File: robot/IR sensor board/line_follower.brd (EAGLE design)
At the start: 8 parts

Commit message: updated schematic and board
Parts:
- JP1: device pinhead:1_05X2MM -> pinhead:1X05
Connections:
- net N$4: now also JP1.2; no longer JP1.3
- net N$5: now also JP1.3; no longer JP1.2
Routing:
- net VCC: track 74.1 -> 70.2 mm
- net GND: track 2.60 -> 0.00 mm
- net N$6: track 18.9 -> 18.2 mm
- net N$4: track 27.1 -> 26.6 mm
- removed copper zone on layer 16, net N$9

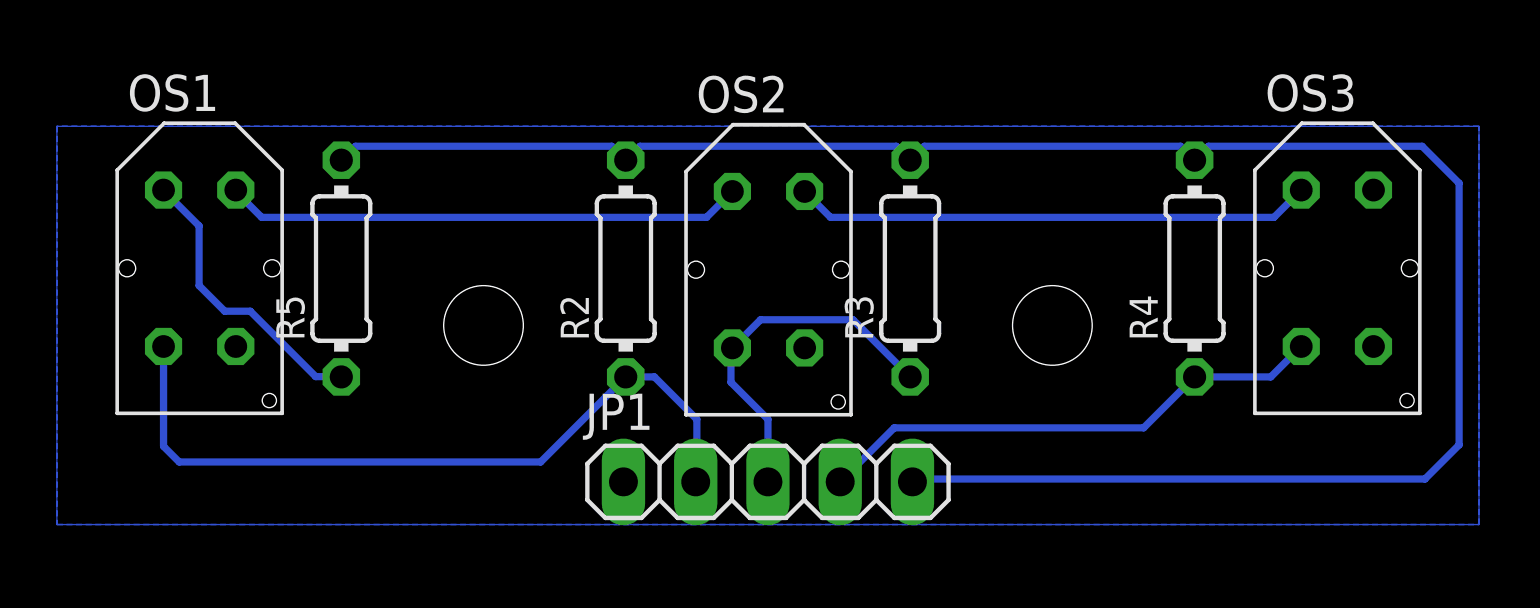
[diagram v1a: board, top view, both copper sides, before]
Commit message: updated sensor board
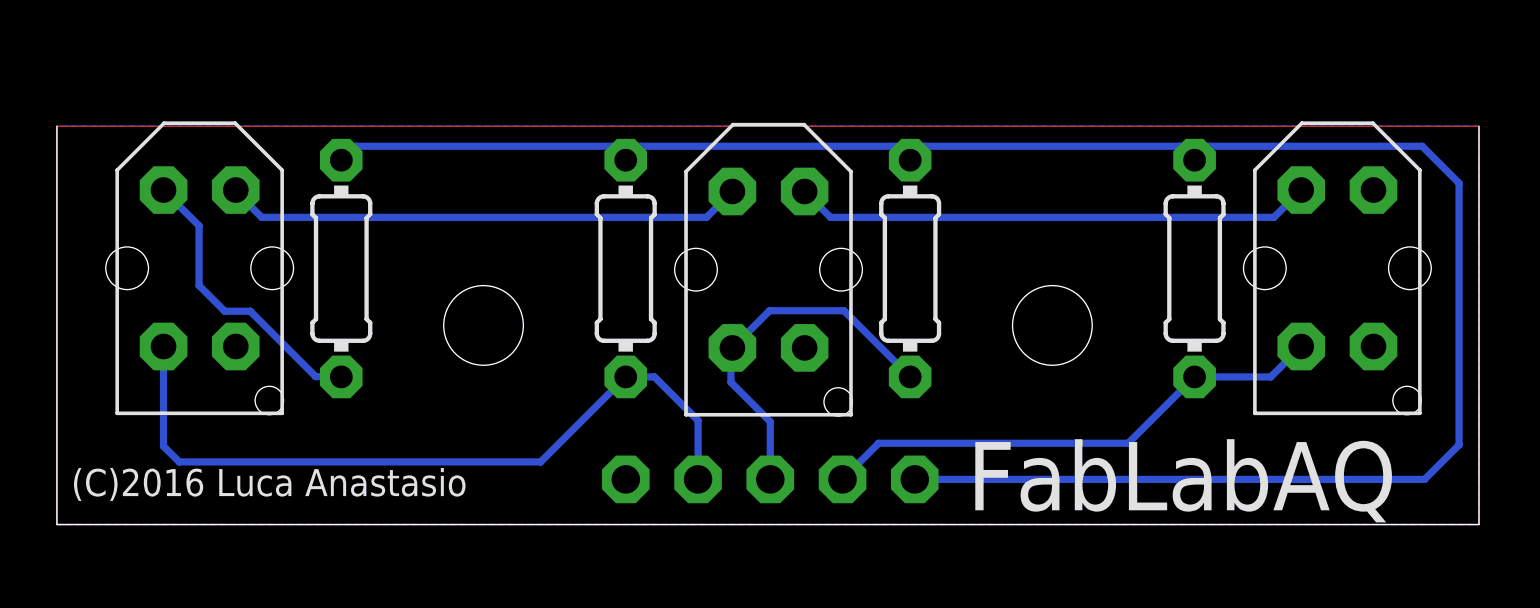
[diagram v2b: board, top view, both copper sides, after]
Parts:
- removed R5: (no value), resistor:0204/7
- added JP2, JP3, JP4, JP5: (no value), pinhead1:1X01
- added R1: 27R, resistor1:0204/7
- JP1: device pinhead:1X05 -> pinhead1:1X01
- R2, R3, R4: value (none) -> 10K; device resistor:0204/7 -> resistor1:0204/7
- moved JP1 5.00 mm to (20.0, 1.59), flipped to the bottom, turned to 90 degrees
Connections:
- net N$3: now also R1.1; no longer R5.1
- net N$4: now also JP2.1; no longer JP1.2
- net N$5: now also JP3.1; no longer JP1.3
- net N$6: now also JP4.1; no longer JP1.4
- net VCC: now also JP5.1, R1.2; no longer JP1.5, R5.2
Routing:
- net N$8: track 0.00 -> 128.0 mm
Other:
- board outline added: 50 x 14 mm
- board text added: "(C)2016 Luca Anastasio"
- board text added: "FabLabAQ"
- board text added: "GND"
- board text added: "VCC"
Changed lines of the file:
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@@
 <setting verticaltext="up"/>
 </settings>
-<grid distance="0.1" unitdist="mm" unit="mm" style="lines" multiple="1" display="no" altdistance="0.025" altunitdist="inch" altunit="inch"/>
+<grid distance="0.5" unitdist="mm" unit="mm" style="lines" multiple="1" display="yes" altdistance="0.025" altunitdist="inch" altunit="inch"/>
 <layers>
 <layer number="1" name="Top" color="4" fill="1" visible="yes" active="yes"/>
@@
 <hole x="15" y="7" drill="2.8"/>
 <hole x="35" y="7" drill="2.8"/>
+<text x="21.2725" y="3.175" size="0.8128" layer="22" font="vector" ratio="10" rot="MR0">GND</text>
+<text x="31.4325" y="3.175" size="0.8128" layer="22" font="vector" ratio="10" rot="MR0">VCC</text>
+<wire x1="0" y1="0" x2="50" y2="0" width="0" layer="46"/>
+<wire x1="50" y1="0" x2="50" y2="14" width="0" layer="46"/>
+<wire x1="0" y1="14" x2="0" y2="0" width="0" layer="46"/>
+<wire x1="0" y1="0" x2="50" y2="0" width="0" layer="47"/>
+<wire x1="50" y1="0" x2="50" y2="14" width="0" layer="47"/>
+<wire x1="50" y1="14" x2="0" y2="14" width="0" layer="47"/>
+<wire x1="0" y1="14" x2="0" y2="0" width="0" layer="47"/>
+<text x="0.5" y="1" size="0.95" layer="21" font="vector" ratio="10">(C)2016 Luca Anastasio</text>
+<text x="32" y="0.5" size="2.4" layer="21" font="vector" ratio="12">FabLabAQ</text>
+<wire x1="0" y1="0" x2="50" y2="0" width="0" layer="48"/>
+<wire x1="50" y1="0" x2="50" y2="14" width="0" layer="48"/>
+<wire x1="50" y1="14" x2="0" y2="14" width="0" layer="48"/>
+<wire x1="0" y1="14" x2="0" y2="0" width="0" layer="48"/>
 </plain>
 <attributes>
@@
 </autorouter>
 <elements>
-<element name="OS1" library="tcrt5000" package="TCRT5000" value="" x="5.02" y="9.01" rot="R270"/>
-<element name="OS2" library="tcrt5000" package="TCRT5000" value="" x="25.02" y="8.96" rot="R270"/>
-<element name="OS3" library="tcrt5000" package="TCRT5000" value="" x="45.02" y="9.01" rot="R270"/>
-<element name="R2" library="resistor" package="0204/7" value="" x="20" y="9" rot="R90"/>
-<element name="R3" library="resistor" package="0204/7" value="" x="30" y="9" rot="R90"/>
-<element name="R4" library="resistor" package="0204/7" value="" x="40" y="9" rot="R90"/>
-<element name="R5" library="resistor" package="0204/7" value="" x="10" y="9" rot="R90"/>
-<element name="JP1" library="pinhead" package="1X05" value="" x="25" y="1.5"/>
+<element name="OS1" library="tcrt5000" package="TCRT5000" value="" x="5.02" y="9.01" smashed="yes" rot="R270">
+<attribute name="VALUE" x="2.48" y="2.31" size="1.27" layer="21"/>
+</element>
+<element name="OS2" library="tcrt5000" package="TCRT5000" value="" x="25.02" y="8.96" smashed="yes" rot="R270">
+<attribute name="VALUE" x="22.48" y="2.26" size="1.27" layer="21"/>
+</element>
+<element name="OS3" library="tcrt5000" package="TCRT5000" value="" x="45.02" y="9.01" smashed="yes" rot="R270">
+<attribute name="VALUE" x="42.48" y="2.31" size="1.27" layer="21"/>
+</element>
+<element name="R2" library="resistor1" package="0204/7" value="10K" x="20" y="9" smashed="yes" rot="R90">
+<attribute name="VALUE" x="20.4826" y="7.3744" size="0.9906" layer="27" font="vector" ratio="10" rot="R90"/>
+</element>
+<element name="R3" library="resistor1" package="0204/7" value="10K" x="30" y="9" smashed="yes" rot="R90">
+<attribute name="VALUE" x="30.4826" y="7.3744" size="0.9906" layer="27" font="vector" ratio="10" rot="R90"/>
+</element>
+<element name="R4" library="resistor1" package="0204/7" value="10K" x="40" y="9" smashed="yes" rot="R90">
+<attribute name="VALUE" x="40.4826" y="7.3744" size="0.9906" layer="27" font="vector" ratio="10" rot="R90"/>
+</element>
+<element name="R1" library="resistor1" package="0204/7" value="27R" x="10" y="9" smashed="yes" rot="R90">
+<attribute name="VALUE" x="10.4826" y="7.3744" size="0.9906" layer="27" font="vector" ratio="10" rot="R90"/>
+</element>
+<element name="JP1" library="pinhead1" package="1X01" value="" x="20.0025" y="1.5875" smashed="yes" rot="MR90">
+<attribute name="VALUE" x="16.8275" y="0.3175" size="1.27" layer="28" rot="MR90"/>
+</element>
+<element name="JP2" library="pinhead1" package="1X01" value="" x="22.5425" y="1.5875" smashed="yes" rot="MR180">
+<attribute name="VALUE" x="21.2725" y="4.7625" size="1.27" layer="28" rot="MR180"/>
+</element>
+<element name="JP3" library="pinhead1" package="1X01" value="" x="25.0825" y="1.5875" smashed="yes" rot="MR180">
+<attribute name="VALUE" x="23.8125" y="4.7625" size="1.27" layer="28" rot="MR180"/>
+</element>
+<element name="JP4" library="pinhead1" package="1X01" value="" x="27.6225" y="1.5875" smashed="yes" rot="MR180">
+<attribute name="VALUE" x="26.3525" y="4.7625" size="1.27" layer="28" rot="MR180"/>
+</element>
+<element name="JP5" library="pinhead1" package="1X01" value="" x="30.1625" y="1.5875" smashed="yes" rot="MR270">
+<attribute name="VALUE" x="33.3375" y="2.8575" size="1.27" layer="28" rot="MR270"/>
+</element>
 </elements>
 <signals>
@@
 <contactref element="OS2" pad="E"/>
 <contactref element="OS1" pad="E"/>
-<contactref element="JP1" pad="1"/>
 <polygon width="0.127" layer="16" isolate="0.127" orphans="yes" rank="6">
 <vertex x="0" y="0"/>
@@
 <vertex x="0" y="14"/>
 </polygon>
+<contactref element="JP1" pad="1"/>
 </signal>
 <signal name="N$3">
-<contactref element="R5" pad="1"/>
+<contactref element="R1" pad="1"/>
 <contactref element="OS1" pad="A"/>
 <wire x1="3.75" y1="11.76" x2="3.75" y2="11.75" width="0.254" layer="16"/>
@@
 </signal>
 <signal name="VCC">
-<contactref element="R5" pad="2"/>
+<contactref element="R1" pad="2"/>
 <contactref element="R2" pad="2"/>
 <contactref element="R3" pad="2"/>
 <contactref element="R4" pad="2"/>
-<contactref element="JP1" pad="5"/>
-<wire x1="48.1" y1="1.6" x2="49.3" y2="2.8" width="0.254" layer="16"/>
+<wire x1="48.0875" y1="1.5875" x2="49.3" y2="2.8" width="0.254" layer="16"/>
 <wire x1="49.3" y1="2.8" x2="49.3" y2="12" width="0.254" layer="16"/>
 <wire x1="49.3" y1="12" x2="48" y2="13.3" width="0.254" layer="16"/>
@@
 <wire x1="10.5" y1="13.3" x2="10.01" y2="12.81" width="0.254" layer="16"/>
 <wire x1="10.01" y1="12.81" x2="10" y2="12.81" width="0.254" layer="16"/>
-<wire x1="48.1" y1="1.6" x2="30.18" y2="1.6" width="0.254" layer="16"/>
-<wire x1="30.18" y1="1.6" x2="30.08" y2="1.5" width="0.254" layer="16"/>
+<contactref element="JP5" pad="1"/>
+<wire x1="48.0875" y1="1.5875" x2="30.1625" y2="1.5875" width="0.254" layer="16"/>
 </signal>
 <signal name="N$4">
 <contactref element="OS1" pad="C"/>
 <contactref element="R2" pad="1"/>
-<contactref element="JP1" pad="2"/>
 <wire x1="3.75" y1="6.26" x2="3.75" y2="2.75" width="0.254" layer="16"/>
 <wire x1="3.75" y1="2.75" x2="4.3" y2="2.2" width="0.254" layer="16"/>
@@
 <wire x1="17.01" y1="2.2" x2="20" y2="5.19" width="0.254" layer="16"/>
 <wire x1="20" y1="5.19" x2="21.01" y2="5.19" width="0.254" layer="16"/>
-<wire x1="21.01" y1="5.19" x2="22.5" y2="3.7" width="0.254" layer="16"/>
-<wire x1="22.5" y1="3.7" x2="22.5" y2="1.54" width="0.254" layer="16"/>
-<wire x1="22.5" y1="1.54" x2="22.46" y2="1.5" width="0.254" layer="16"/>
+<contactref element="JP2" pad="1"/>
+<wire x1="21.01" y1="5.19" x2="22.5425" y2="3.6575" width="0.254" layer="16"/>
+<wire x1="22.5425" y1="3.6575" x2="22.5425" y2="1.5875" width="0.254" layer="16"/>
 </signal>
 <signal name="N$5">
 <contactref element="OS2" pad="C"/>
 <contactref element="R3" pad="1"/>
-<contactref element="JP1" pad="3"/>
-<wire x1="25" y1="1.5" x2="25" y2="3.7" width="0.254" layer="16"/>
-<wire x1="25" y1="3.7" x2="23.7" y2="5" width="0.254" layer="16"/>
 <wire x1="23.7" y1="5" x2="23.7" y2="6.16" width="0.254" layer="16"/>
 <wire x1="23.7" y1="6.16" x2="23.75" y2="6.21" width="0.254" layer="16"/>
-<wire x1="30" y1="5.19" x2="27.99" y2="7.2" width="0.254" layer="16"/>
-<wire x1="27.99" y1="7.2" x2="24.74" y2="7.2" width="0.254" layer="16"/>
-<wire x1="24.74" y1="7.2" x2="23.75" y2="6.21" width="0.254" layer="16"/>
+<wire x1="30" y1="5.19" x2="27.6725" y2="7.5175" width="0.254" layer="16"/>
+<wire x1="27.6725" y1="7.5175" x2="25.0575" y2="7.5175" width="0.254" layer="16"/>
+<wire x1="25.0575" y1="7.5175" x2="23.75" y2="6.21" width="0.254" layer="16"/>
+<contactref element="JP3" pad="1"/>
+<wire x1="23.7" y1="5" x2="25.0825" y2="3.6175" width="0.254" layer="16"/>
+<wire x1="25.0825" y1="3.6175" x2="25.0825" y2="1.5875" width="0.254" layer="16"/>
 </signal>
 <signal name="N$6">
 <contactref element="OS3" pad="C"/>
 <contactref element="R4" pad="1"/>
-<contactref element="JP1" pad="4"/>
-<wire x1="40" y1="5.19" x2="38.21" y2="3.4" width="0.254" layer="16"/>
+<wire x1="40" y1="5.19" x2="37.6675" y2="2.8575" width="0.254" layer="16"/>
 <wire x1="40" y1="5.19" x2="42.68" y2="5.19" width="0.254" layer="16"/>
 <wire x1="42.68" y1="5.19" x2="43.75" y2="6.26" width="0.254" layer="16"/>
-<wire x1="38.21" y1="3.4" x2="29.44" y2="3.4" width="0.254" layer="16"/>
-<wire x1="29.44" y1="3.4" x2="27.54" y2="1.5" width="0.254" layer="16"/>
+<contactref element="JP4" pad="1"/>
+<wire x1="37.6675" y1="2.8575" x2="28.8925" y2="2.8575" width="0.254" layer="16"/>
+<wire x1="28.8925" y1="2.8575" x2="27.6225" y2="1.5875" width="0.254" layer="16"/>
 </signal>
 <signal name="N$7">
@@
 <wire x1="0" y1="14" x2="0" y2="0" width="0" layer="16"/>
 </signal>
+<signal name="N$8">
+<wire x1="0" y1="0" x2="50" y2="0" width="0" layer="1"/>
+<wire x1="50" y1="0" x2="50" y2="14" width="0" layer="1"/>
+<wire x1="50" y1="14" x2="0" y2="14" width="0" layer="1"/>
+<wire x1="0" y1="14" x2="0" y2="0" width="0" layer="1"/>
+</signal>
 </signals>
